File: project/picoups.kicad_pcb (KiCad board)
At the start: 4 copper layers, 65 x 30 mm, 64 parts, among them J1 VIN, J2 BATT, J3 USB_C_Receptacle, J4 Conn_02x20_Odd_Even, Q1 Q_PMOS_GSD, SW1 SW_5V, SW2 SW_USER, U1 LT3652EMSE, U2 TPS2116, U3 TPS61235P, U4 BQ24040, U5 INA3221, U6 M41T62

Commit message: Added labels
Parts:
- moved JP4 5.40 mm to (151.8, 113.8)
- moved JP5 5.40 mm to (151.8, 100.2)
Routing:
- net /Status LEDs/USB_PWRGD: track 32.5 -> 35.8 mm
- net /Status LEDs/USB_CHRG: track 33.1 -> 36.3 mm
- net Net-(D7-K): track 5.27 -> 4.74 mm
- net Net-(D6-K): track 5.27 -> 4.74 mm
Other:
- board text added: "CHARGE"
- board text added: "FAULT"
- board text added: "PWRGD"
- board text added: "USER BTN"

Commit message: Added final labels
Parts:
- added G***: LOGO, PicoUPS:Logo_Front_Silk, F.Cu at (105.0, 111.0)
- added G***: LOGO, PicoUPS:Logo_Front_Mask, F.Cu at (105.0, 111.0)
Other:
- board text added: "- + BATT JST-PH"
- board text added: "- + SOLAR JST-PH"
- board text added: "750mA"

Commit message: Final touches
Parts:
- added G***: LOGO, PicoUPS:MY-Logo_4.5x10mm_SolderMask, B.Cu at (105.2, 111.2)
- added G***: LOGO, PicoUPS:Logo_KiCad, B.Cu at (100.8, 108.2)
- added REF**: OSHW-Logo_5.7x6mm_SilkScreen, Symbol:OSHW-Logo_5.7x6mm_SilkScreen, B.Cu at (101.2, 118.0)
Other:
- outline, holes or cut-outs redrawn
- board text added: "G"
- board text added: "PicoUPS"
- board text added: "V"
- board text added: "rev 1.0.0 28.07.23 Διονύσης Τουλάτος"
- board text added: "v1"

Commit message: Final revision
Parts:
- moved JP2 0.10 mm to (137.4, 120.0)
- moved JP3 0.10 mm to (140.0, 120.0)
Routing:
- net GND: vias 32 -> 66

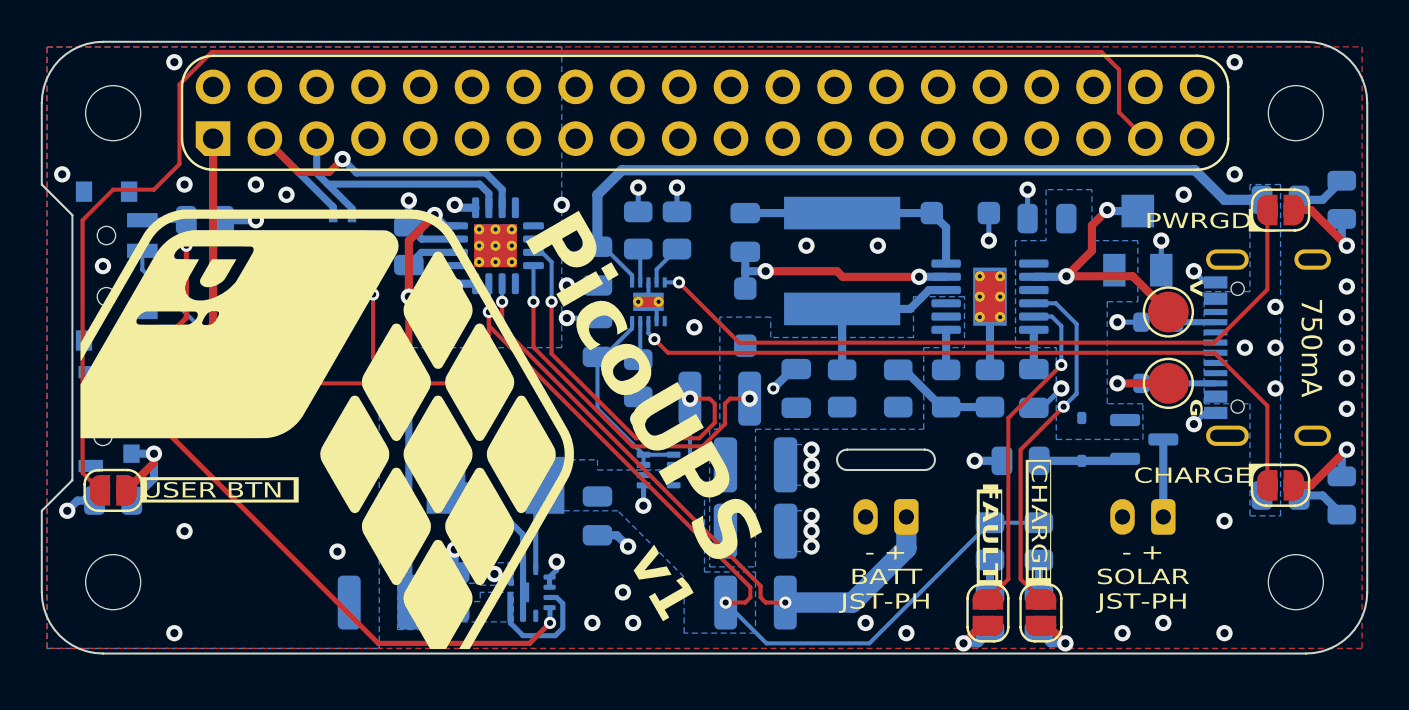
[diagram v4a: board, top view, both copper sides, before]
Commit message: Fixed mirrored RTC footprint
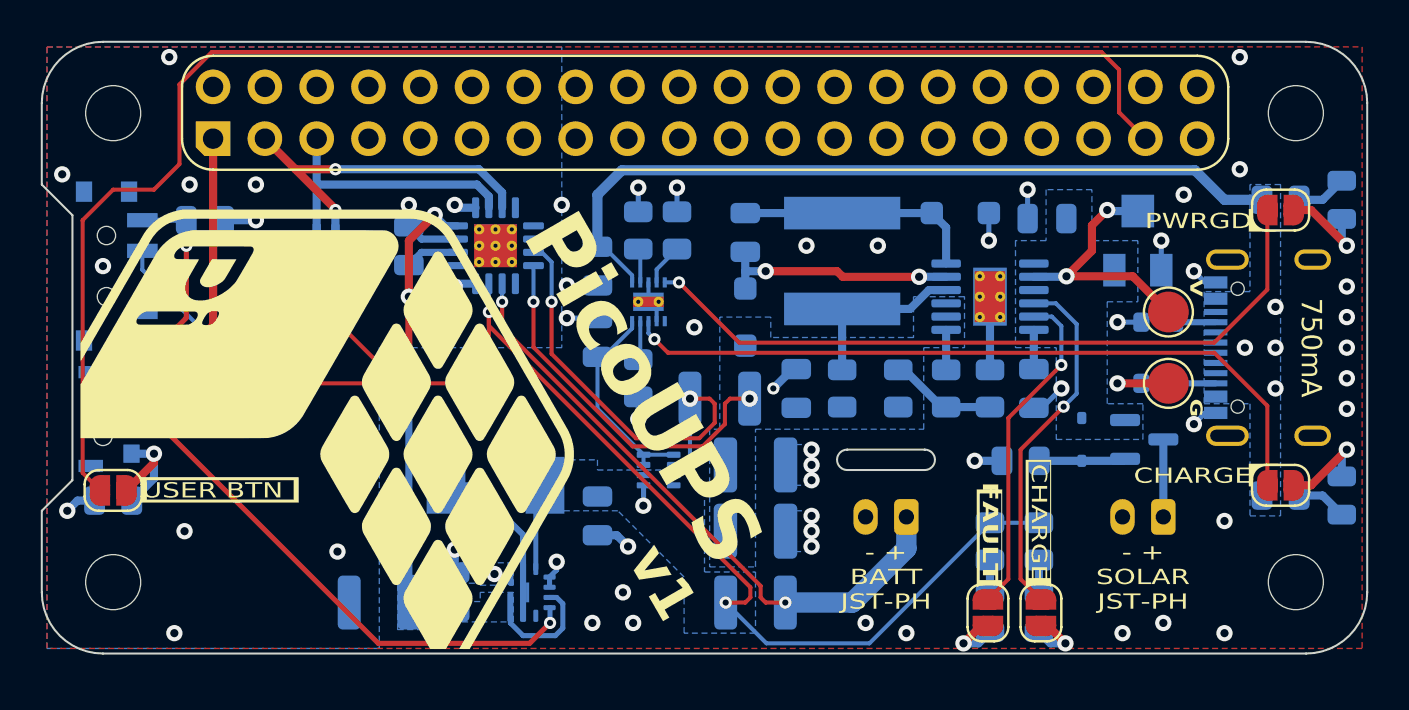
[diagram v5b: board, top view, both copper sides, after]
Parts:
- moved U6 0.95 mm to (104.9, 102.5)
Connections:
- U4 pad 11: GND -> (no net)
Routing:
- net SDA: track 19.4 -> 17.2 mm, vias 1 -> 2
- net GND: track 43.8 -> 43.7 mm, vias 66 -> 65

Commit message: Minor improvements
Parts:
- added TP3: 5V, TestPoint:TestPoint_Pad_D1.0mm, B.Cu at (107.5, 107.0)
- added TP4: GND, TestPoint:TestPoint_Pad_D1.0mm, B.Cu at (107.5, 109.0)
- added TP5: GND, TestPoint:TestPoint_Pad_D1.0mm, B.Cu at (120.5, 118.2)
- added TP6: VBAT, TestPoint:TestPoint_Pad_D1.0mm, B.Cu at (122.5, 118.2)
- added TP8: VBAT, TestPoint:TestPoint_Pad_D1.0mm, B.Cu at (123.0, 106.0)
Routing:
- net VBAT_SOL-: track 21.7 -> 25.3 mm
- net GND: track 43.7 -> 46.7 mm, vias 65 -> 63
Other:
- board text added: "5V"
- board text added: "GND"
- board text added: "SOL"
- board text added: "VBAT"

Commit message: Semi final v1.1
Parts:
- removed R15: 1M, Resistor_SMD:R_0805_2012Metric
- R18, R19: value 260 -> 500
- moved R5 0.75 mm to (98.2, 100.8), turned to -90 degrees
- moved G*** 0.20 mm to (105.0, 110.8) (x2)
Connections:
- JP1 pad 1: Net-(JP1-A) -> SCL
- SW2 pad 1: 3v3 -> GND
- SW2 pad 2: Net-(JP1-A) -> SCL
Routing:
- net SCL: track 13.6 -> 32.5 mm, vias 0 -> 3
- net 3v3: track 14.4 -> 0.00 mm, vias 1 -> 0
- net Net-(SW1-C): track 38.5 -> 31.7 mm
- net Net-(JP1-A): track 6.21 -> 0.00 mm, vias 1 -> 0
- net Net-(D4-K): track 3.09 -> 0.00 mm
- net Net-(D5-K): track 3.09 -> 0.00 mm
- net Net-(D7-K): track 4.74 -> 2.53 mm
- net Net-(D6-K): track 4.74 -> 2.53 mm
- net GND: track 46.7 -> 45.6 mm, vias 63 -> 61
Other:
- board text added: "rev 1.1.0 27.08.23 Διονύσης Τουλάτος"
- board text added: "v1.1"
- board text removed: "rev 1.0.0 28.07.23 Διονύσης Τουλάτος"
- board text removed: "v1"

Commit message: Revision 1.1.1
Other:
- outline, holes or cut-outs redrawn
- board text added: "rev 1.1.1 16.09.23 Διονύσης Τουλάτος"
- board text removed: "rev 1.1.0 27.08.23 Διονύσης Τουλάτος"
